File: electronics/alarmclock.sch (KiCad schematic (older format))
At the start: 20 parts, among them J1 SWD, J2 AudioJack2, J3 Conn_02x11_Odd_Even, J4 Conn_01x08, J5 Conn_01x08, SW1 Reset, SW2 Rotary_Encoder_Switch, U1 STM32F030C6T6, Y1 24MHz

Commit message: feature: new microprossesor for beter low power performance and smaller footprint
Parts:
- removed C5: 1uF, Capacitor_SMD:C_1206_3216Metric, symbol Device:C_Small
- removed C6: 10nF, Capacitor_SMD:C_1206_3216Metric, symbol Device:C_Small
- removed J3: Conn_02x11_Odd_Even, Connector_PinHeader_2.54mm:PinHeader_2x11_P2.54mm_Vertical, symbol Connector_Generic:Conn_02x11_Odd_Even
- removed U1: STM32F030C6T6, Package_QFP:LQFP-48_7x7mm_P0.5mm, symbol MCU_ST_STM32F0:STM32F030C6Tx
- added J3, J6: Conn_02x08_Top_Bottom, Connector_PinHeader_2.54mm:PinHeader_2x08_P2.54mm_Vertical, symbol Connector_Generic:Conn_02x08_Top_Bottom
- added U1: STM32L011K4T6, Package_QFP:LQFP-32_7x7mm_P0.8mm, symbol MCU_ST_STM32L0:STM32L011K4Tx
- BZ1: footprint (none) -> Connector_PinHeader_2.54mm:PinHeader_1x02_P2.54mm_Vertical
- J2: footprint Connector_Audio:Jack_3.5mm_CUI_SJ-3523-SMT_Horizontal -> Connector_PinHeader_2.54mm:PinHeader_1x02_P2.54mm_Vertical
- SW2: footprint (none) -> Connector_PinHeader_1.00mm:PinHeader_1x06_P1.00mm_Vertical
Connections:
- net labels removed: BOOT0
- wire segments 121 -> 120
- no-connect marks 8 -> 9
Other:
- moved on the sheet: J4, J5, SW1, SW2

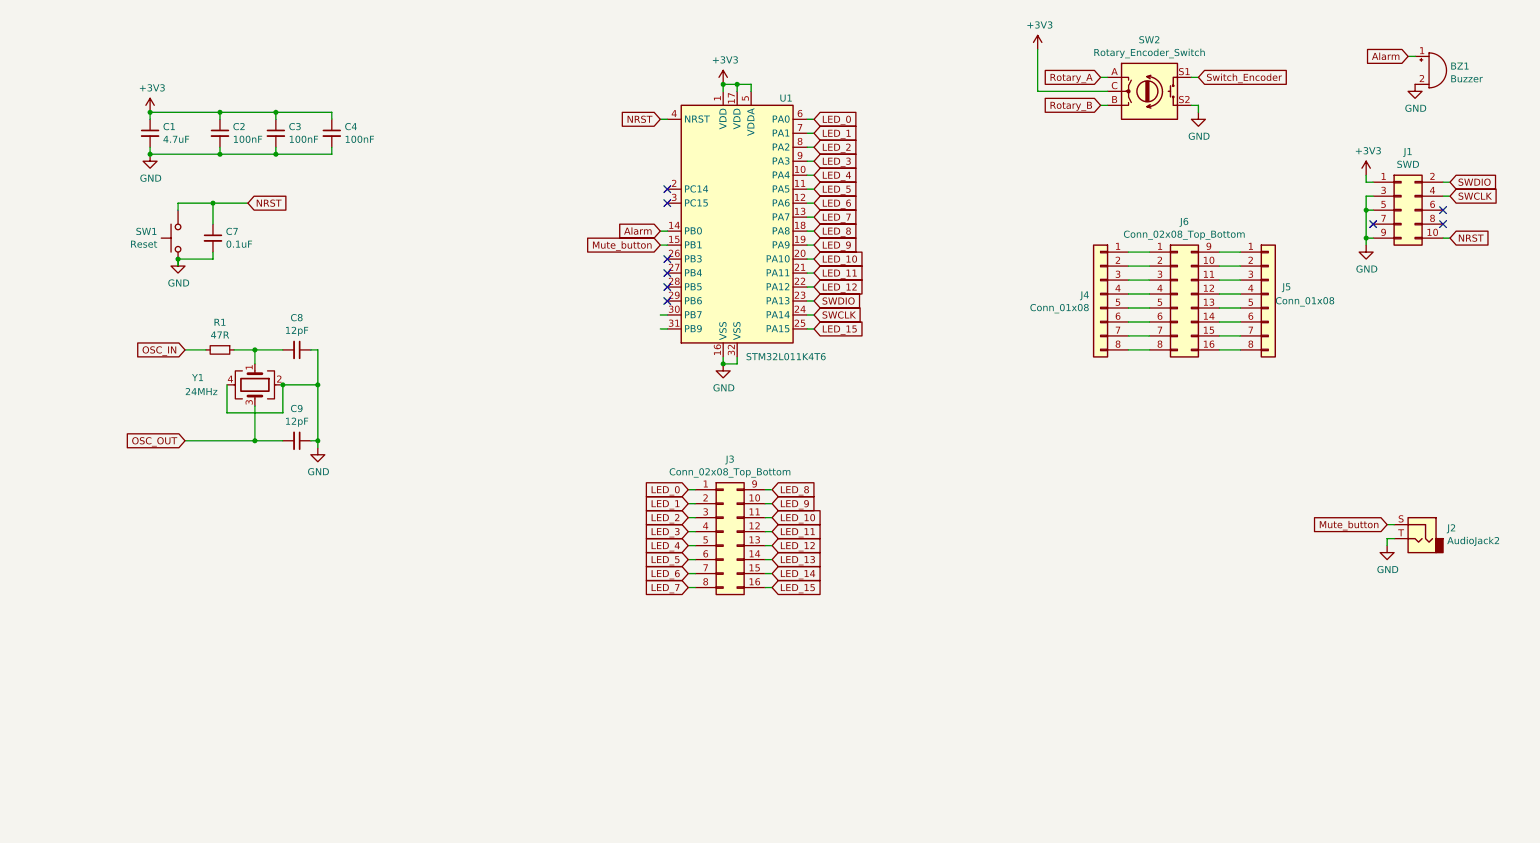
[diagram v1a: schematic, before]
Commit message: added beginning of battery backup
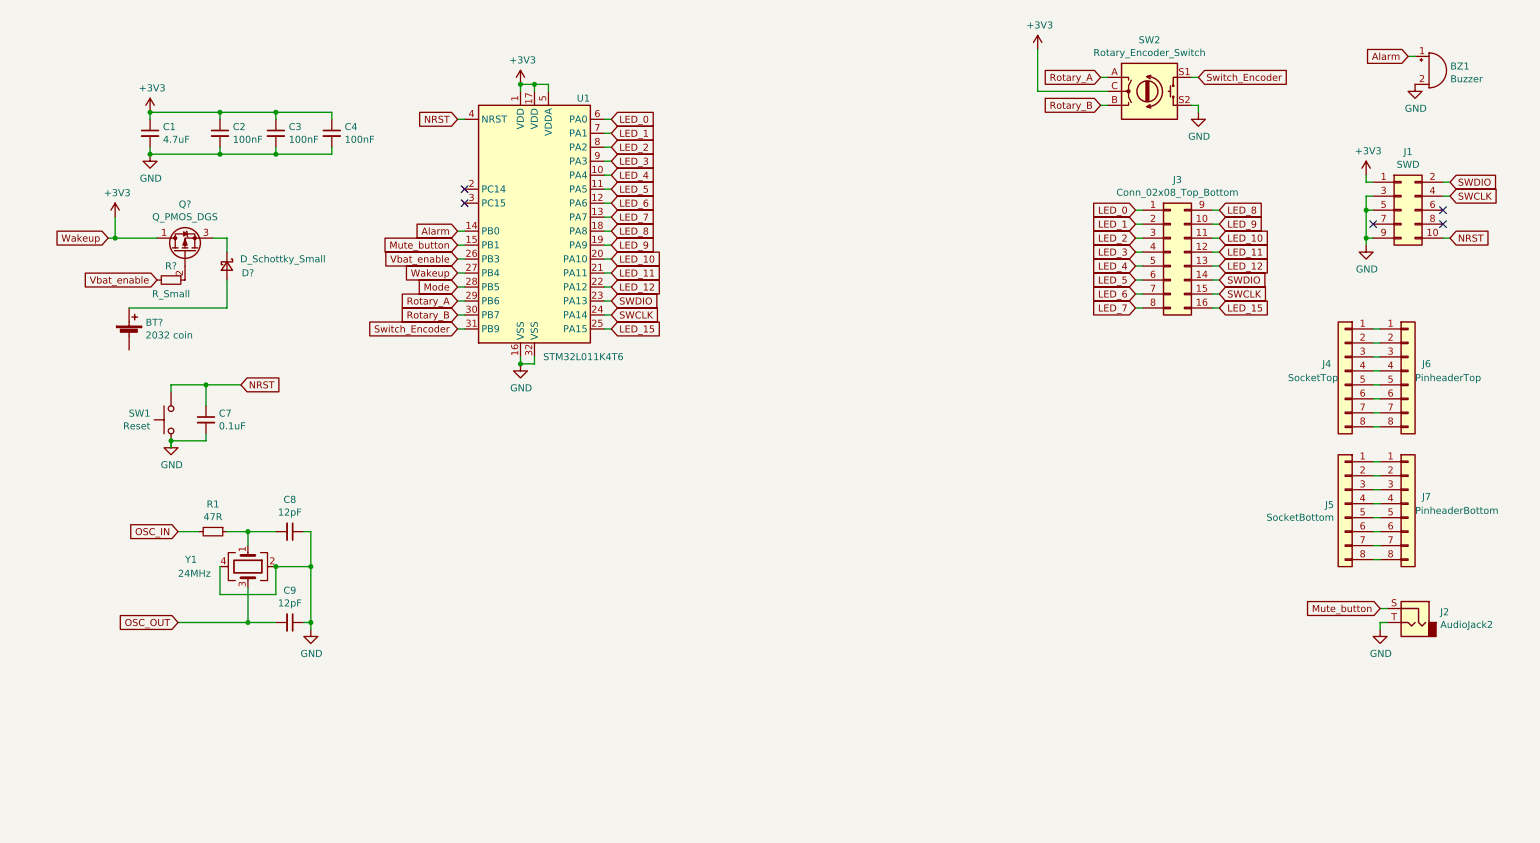
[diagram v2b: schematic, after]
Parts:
- removed J6: Conn_02x08_Top_Bottom, Connector_PinHeader_2.54mm:PinHeader_2x08_P2.54mm_Vertical, symbol Connector_Generic:Conn_02x08_Top_Bottom
- added BT?: 2032 coin, symbol Device:Battery_Cell
- added D?: D_Schottky_Small, symbol Device:D_Schottky_Small
- added J4: SocketTop, Connector_PinSocket_2.54mm:PinSocket_1x08_P2.54mm_Vertical, symbol Connector_Generic:Conn_01x08
- added J7: PinheaderBottom, Connector_PinHeader_2.54mm:PinHeader_1x08_P2.54mm_Vertical, symbol Connector_Generic:Conn_01x08
- added Q?: Q_PMOS_DGS, symbol Device:Q_PMOS_DGS
- added R?: R_Small, symbol Device:R_Small
- J5: renamed from J4; value Conn_01x08 -> SocketBottom
- J6: renamed from J5; value Conn_01x08 -> PinheaderTop; footprint Connector_PinSocket_2.54mm:PinSocket_1x08_P2.54mm_Vertical -> Connector_PinHeader_2.54mm:PinHeader_1x08_P2.54mm_Vertical
- SW1: footprint Button_Switch_SMD:SW_DIP_SPSTx01_Slide_9.78x4.72mm_W8.61mm_P2.54mm -> Connector_PinHeader_2.54mm:PinHeader_1x02_P2.54mm_Vertical
- SW2: footprint Connector_PinHeader_1.00mm:PinHeader_1x06_P1.00mm_Vertical -> Connector_PinHeader_2.54mm:PinHeader_1x05_P2.54mm_Vertical
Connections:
- net LED_13 is gone; now on net SWDIO: J3.14 (Pin_14)
- net LED_14 is gone; now on net SWCLK: J3.15 (Pin_15)
- net +3V3: now also U1.27 (PB4), Q?.1 (D)
- net Rotary_A: now also U1.29 (PB6)
- net Rotary_B: now also U1.30 (PB7)
- net Switch_Encoder: now also U1.31 (PB9)
- net at J5.1 (Pin_1): now also J7.1 (Pin_1)
- net at J5.2 (Pin_2): now also J7.2 (Pin_2)
- net at J5.3 (Pin_3): now also J7.3 (Pin_3)
- net at J5.4 (Pin_4): now also J7.4 (Pin_4)
- net at J5.5 (Pin_5): now also J7.5 (Pin_5)
- net at J5.6 (Pin_6): now also J7.6 (Pin_6)
- net at J5.7 (Pin_7): now also J7.7 (Pin_7)
- net at J5.8 (Pin_8): now also J7.8 (Pin_8)
- net at J6.1 (Pin_1): now also J4.1 (Pin_1)
- net at J6.2 (Pin_2): now also J4.2 (Pin_2)
- net at J6.3 (Pin_3): now also J4.3 (Pin_3)
- net at J6.4 (Pin_4): now also J4.4 (Pin_4)
- net at J6.5 (Pin_5): now also J4.5 (Pin_5)
- net at J6.6 (Pin_6): now also J4.6 (Pin_6)
- net at J6.7 (Pin_7): now also J4.7 (Pin_7)
- net at J6.8 (Pin_8): now also J4.8 (Pin_8)
- net Vbat_enable: now reaches U1.26 (PB3)
- net Vbat_enable: now also R?.2
- net Mode: now reaches U1.28 (PB5)
- new net: BT?.1 (+), D?.2 (A)
- new net: D?.1 (K), Q?.3 (S)
- new net: Q?.2 (G), R?.1
- no-connect marks 9 -> 5
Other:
- moved on the sheet: C7, C8, C9, J2, J3, J5, J6, R1, SW1, U1, Y1

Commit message: minor changes
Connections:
- net GND: now also BT?.2 (-)
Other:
- moved on the sheet: BT?, D?, Q?, R?, U1

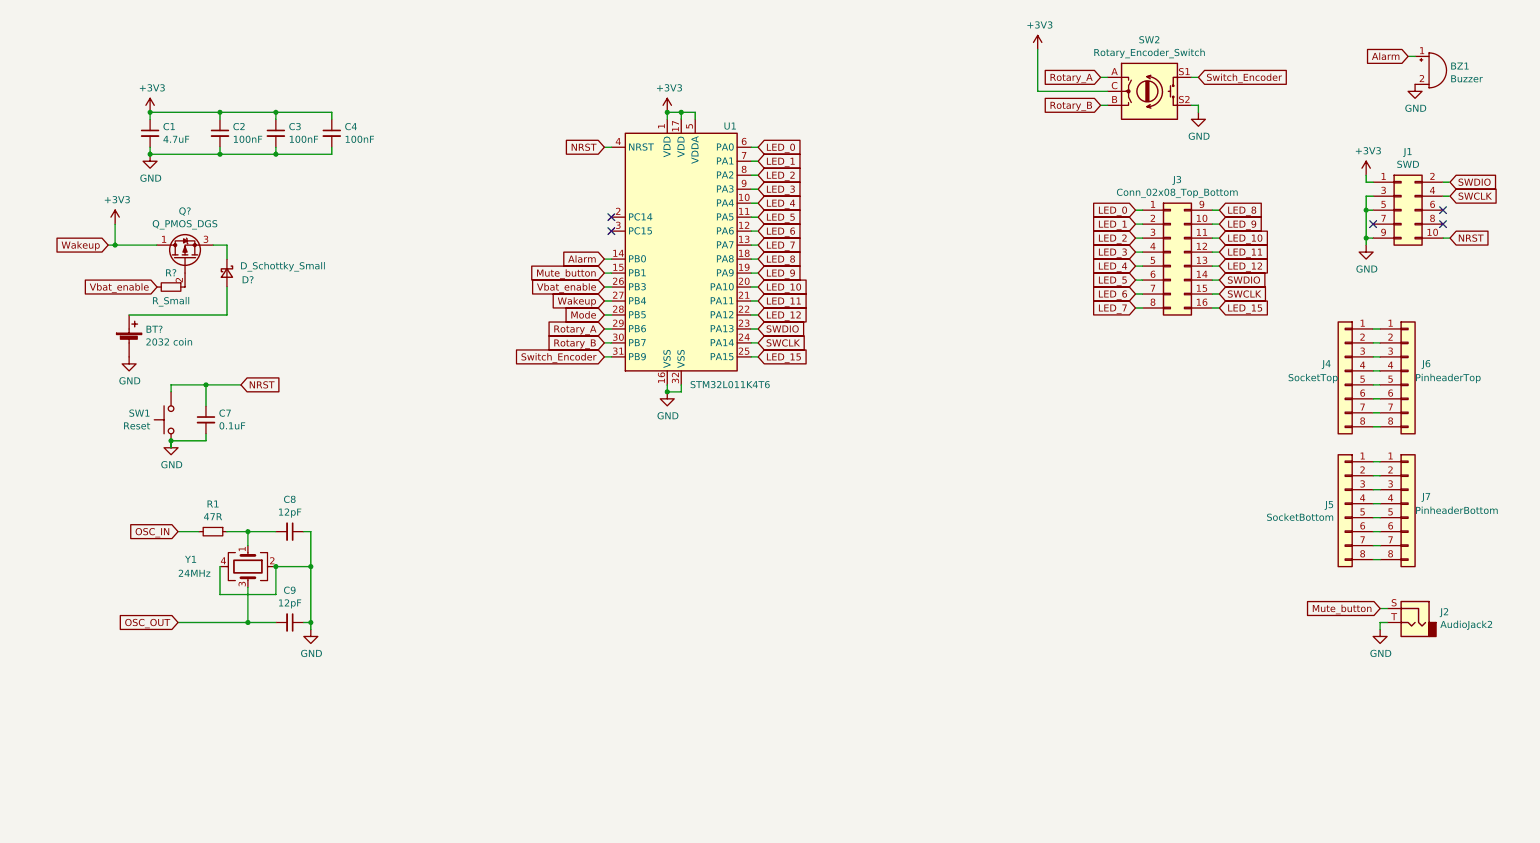
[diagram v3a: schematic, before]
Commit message: yet another microcontroller switch. added shiftregisters, added battery backup
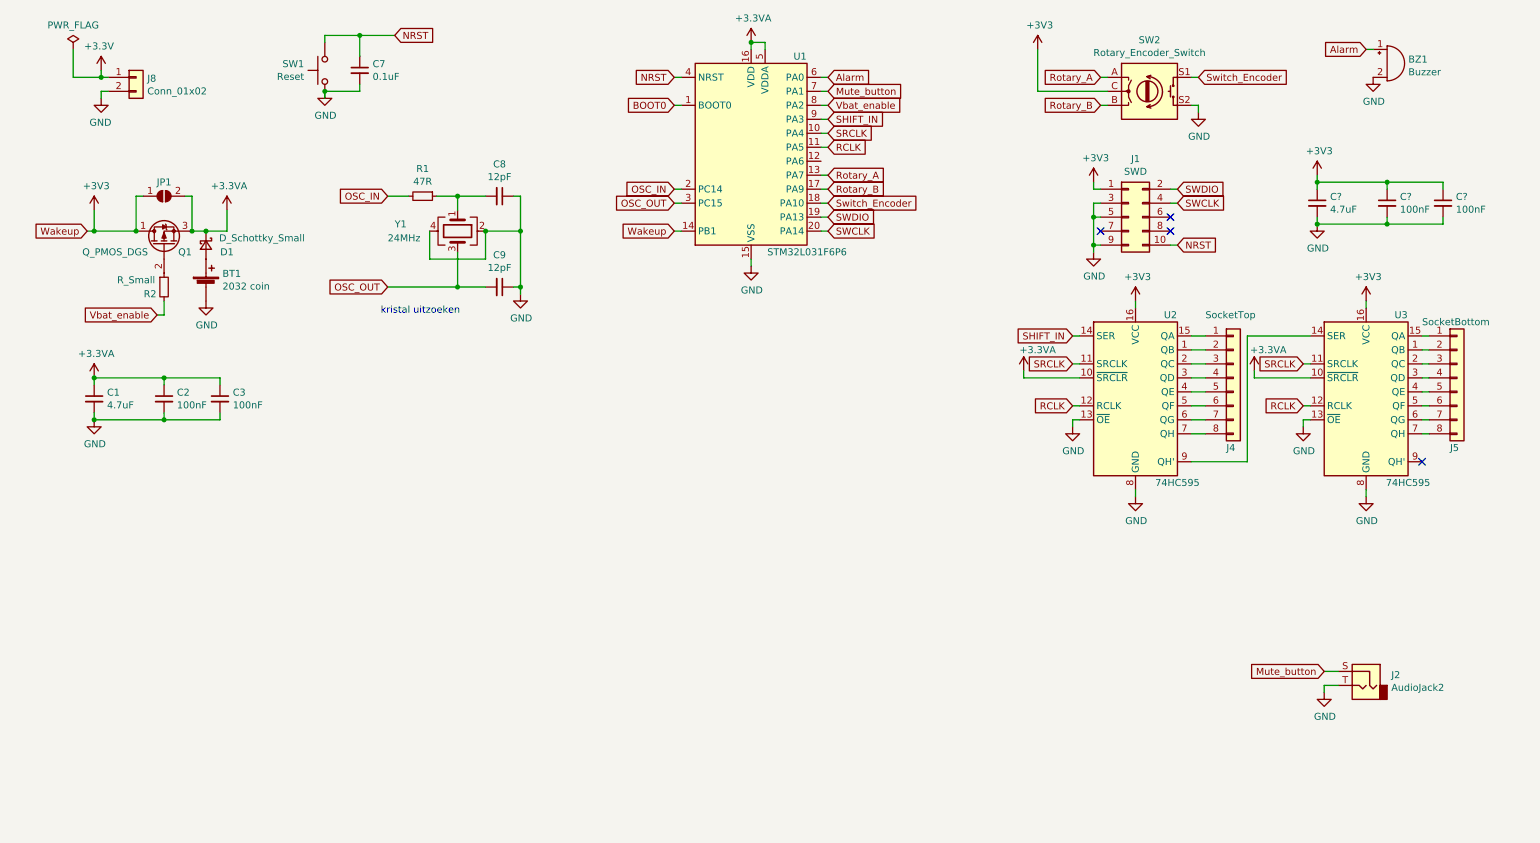
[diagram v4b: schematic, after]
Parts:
- removed C4: 100nF, Capacitor_SMD:C_1206_3216Metric, symbol Device:C_Small
- removed J3: Conn_02x08_Top_Bottom, Connector_PinHeader_2.54mm:PinHeader_2x08_P2.54mm_Vertical, symbol Connector_Generic:Conn_02x08_Top_Bottom
- removed J6: PinheaderTop, Connector_PinHeader_2.54mm:PinHeader_1x08_P2.54mm_Vertical, symbol Connector_Generic:Conn_01x08
- removed J7: PinheaderBottom, Connector_PinHeader_2.54mm:PinHeader_1x08_P2.54mm_Vertical, symbol Connector_Generic:Conn_01x08
- removed U1: STM32L011K4T6, Package_QFP:LQFP-32_7x7mm_P0.8mm, symbol MCU_ST_STM32L0:STM32L011K4Tx
- added C?: 4.7uF, Capacitor_SMD:C_1206_3216Metric, symbol Device:C_Small
- added C? (x2): 100nF, Capacitor_SMD:C_1206_3216Metric, symbol Device:C_Small
- added J8: Conn_01x02, symbol Connector_Generic:Conn_01x02
- added JP1: SolderJumper_2_Open, symbol Jumper:SolderJumper_2_Open
- added U1: STM32L031F6P6, Package_SO:TSSOP-20_4.4x6.5mm_P0.65mm, symbol MCU_ST_STM32L0:STM32L031F6Px
- added U2, U3: 74HC595, symbol 74xx:74HC595
- gave numbers to parts that had none: 4
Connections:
- net +3V3: now also C?.1, C?.1, C?.1, J8.1 (Pin_1), JP1.1 (A), U1.14 (PB1), U2.16 (VCC), U3.16 (VCC); no longer C1.1, C2.1, C3.1
- net Alarm: now also U1.6 (PA0)
- net GND: now also C?.2, C?.2, C?.2, J8.2 (Pin_2), U1.15 (VSS), U2.13 (~OE), U2.8 (GND), U3.13 (~OE), U3.8 (GND)
- net Mute_button: now also U1.7 (PA1)
- net NRST: now also U1.4 (NRST)
- net OSC_IN: now also U1.2 (PC14)
- net OSC_OUT: now also U1.3 (PC15)
- net Rotary_A: now also U1.13 (PA7)
- net Rotary_B: now also U1.17 (PA9)
- net SWCLK: now also U1.20 (PA14)
- net SWDIO: now also U1.19 (PA13)
- net Switch_Encoder: now also U1.18 (PA10)
- net Vbat_enable: now also U1.8 (PA2)
- net at J5.1 (Pin_1): now also U3.15 (QA)
- net at J5.2 (Pin_2): now also U3.1 (QB)
- net at J5.3 (Pin_3): now also U3.2 (QC)
- net at J5.4 (Pin_4): now also U3.3 (QD)
- net at J5.5 (Pin_5): now also U3.4 (QE)
- net at J5.6 (Pin_6): now also U3.5 (QF)
- net at J5.7 (Pin_7): now also U3.6 (QG)
- net at J5.8 (Pin_8): now also U3.7 (QH)
- net at J4.1 (Pin_1): now also U2.15 (QA)
- net at J4.2 (Pin_2): now also U2.1 (QB)
- net at J4.3 (Pin_3): now also U2.2 (QC)
- net at J4.4 (Pin_4): now also U2.3 (QD)
- net at J4.5 (Pin_5): now also U2.4 (QE)
- net at J4.6 (Pin_6): now also U2.5 (QF)
- net at J4.7 (Pin_7): now also U2.6 (QG)
- net at J4.8 (Pin_8): now also U2.7 (QH)
- net +3.3VA: now reaches D1.1 (K), Q1.3 (S)
- net +3.3VA: now also C1.1, C2.1, C3.1, JP1.2 (B), U1.16 (VDD), U1.5 (VDDA), U2.10 (~SRCLR), U3.10 (~SRCLR)
- new net: U2.9 (QH'), U3.14 (SER)
- new net BOOT0: U1.1 (BOOT0)
- new net RCLK: U1.11 (PA5), U2.12 (RCLK), U3.12 (RCLK)
- new net SHIFT_IN: U1.9 (PA3), U2.14 (SER)
- new net SRCLK: U1.10 (PA4), U2.11 (SRCLK), U3.11 (SRCLK)
- no-connect marks 5 -> 4
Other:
- note added: "kristal uitzoeken\n"
- moved on the sheet: BT1, BZ1, C1, C2, C3, C7, C8, C9, D1, J1, J2, J4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

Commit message: add 5v rail and voltage regulator
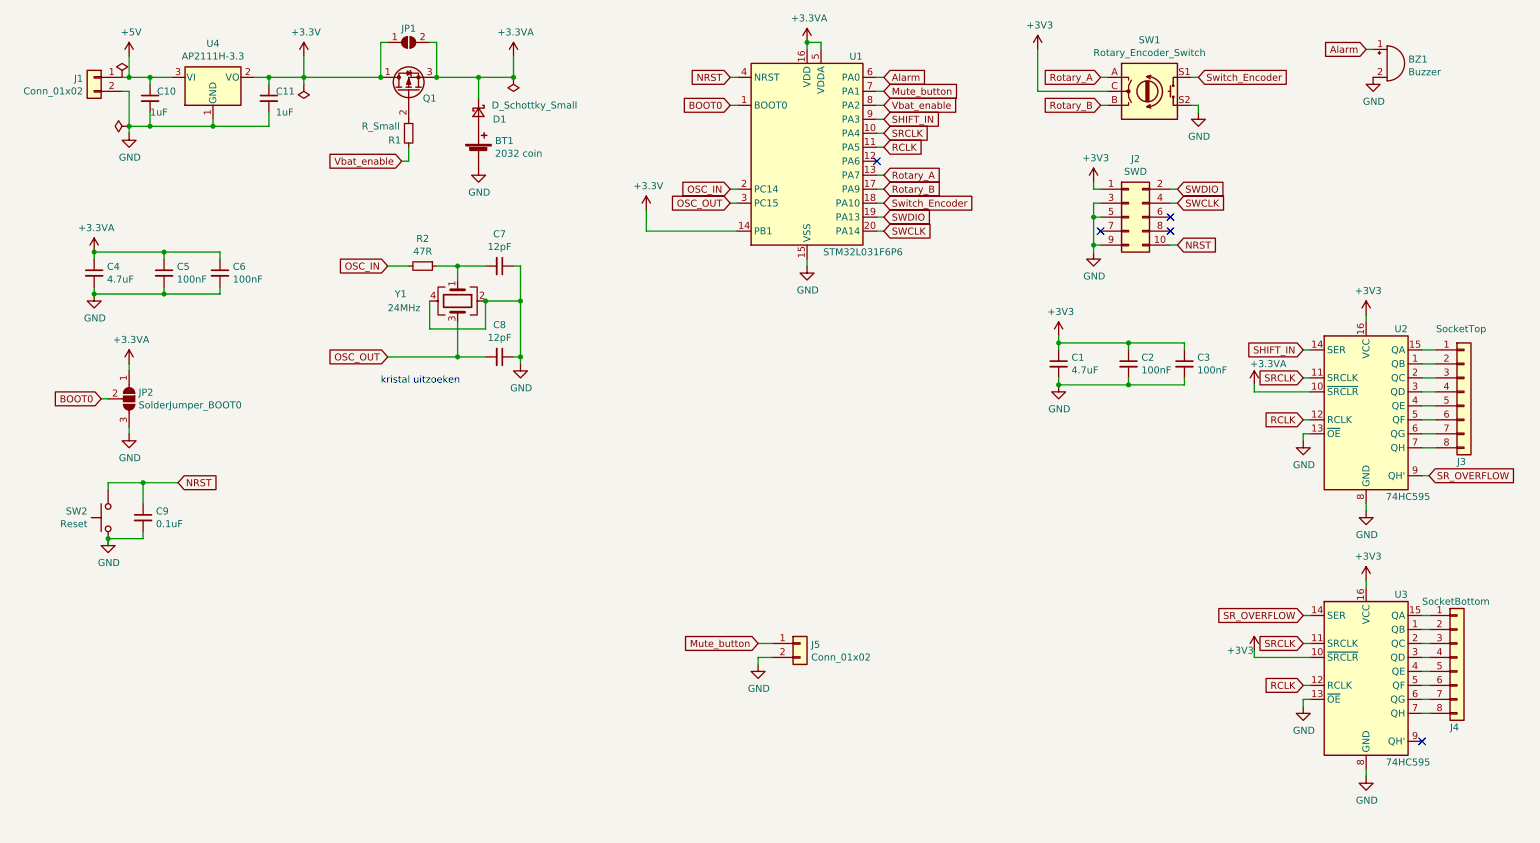
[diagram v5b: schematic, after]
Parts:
- removed J2: AudioJack2, Connector_PinHeader_2.54mm:PinHeader_1x02_P2.54mm_Vertical, symbol Connector:AudioJack2
- added C10, C11: 1uF, Capacitor_SMD:C_1206_3216Metric, symbol Device:C_Small
- added J5: Conn_01x02, symbol Connector_Generic:Conn_01x02
- added JP2: SolderJumper_BOOT0, symbol Jumper:SolderJumper_3_Open
- added U4: AP2111H-3.3, Package_TO_SOT_SMD:SOT-223-3_TabPin2, symbol Regulator_Linear:NCP1117-3.3_SOT223
- Q1: value Q_PMOS_DGS -> Backpower
- gave numbers to parts that had none: 3
- renumbered C1 to C4, C2 to C5, C3 to C6, C8 to C7, C9 to C8, C7 to C9, J8 to J1, J1 to J2, J4 to J3, J5 to J4, R2 to R1, R1 to R2, SW2 to SW1, SW1 to SW2
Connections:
- net +3.3VA: now also JP2.1 (A); no longer U3.10 (~SRCLR)
- net +3V3: now also U3.10 (~SRCLR), C11.1, U4.2 (VO); no longer J1.1 (Pin_1)
- net BOOT0: now also JP2.2 (C)
- net GND: now also C10.2, C11.2, J5.2 (Pin_2), JP2.3 (B), U4.1 (GND)
- net Mute_button: now also J5.1 (Pin_1)
- net SR_OVERFLOW: now reaches U2.9 (QH'), U3.14 (SER)
- new net +5V: C10.1, J1.1 (Pin_1), U4.3 (VI)
- no-connect marks 4 -> 5
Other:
- moved on the sheet: BT1, C1, C2, C3, C4, C5, C6, C7, C8, C9, D1, J1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
